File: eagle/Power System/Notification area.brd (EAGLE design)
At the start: 114 x 80 mm, 53 parts, among them IC3 LM358N, T7 2N2222

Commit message: PCB layout beta
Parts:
- removed D5, D6, D7, D8: 1N4004, diode:DO41-10
- removed S1, S2: RDT1034, switch:RDT1034
- removed S4: TL32PO, switch:TL3XPO
- added C8, C9: 2uF, capacitor-wima:C2.5-3
- added LED_A: BLUE, display-hp:HLMP6
- added LED_B, LED_D: GREEN, display-hp:HLMP6
- added LED_C: RED, display-hp:HLMP6
- added PAD3: Power +, wirepad:5-2,5
- added PAD4: Power -, wirepad:5-2,5
- added SV2: (no value), con-lstb:MA03-1
- added U$1, U$2, U$4: (no value), holes:3,0
- C4, C7: value 1uF -> 2uF
- D1, D2: value HLMP6 -> 1N4001; device display-hp:HLMP6 -> diode:DO41-10
- D3, D4: value HLMP6 -> 1N4004; device display-hp:HLMP6 -> diode:DO41-10
- PAD1: value WIREPADSMD5-2,5 -> Motor +
- PAD2: value WIREPADSMD5-2,5 -> Motor -
- moved D9 211.0 mm to (99.1, 38.1)
- moved R20 206.5 mm to (67.3, 62.2)
- moved R18 188.6 mm to (67.3, 57.1), turned to 180 degrees
- moved R16 183.4 mm to (57.1, 64.8), turned to 180 degrees
- moved R14 177.6 mm to (57.1, 59.7), turned to 180 degrees
- moved R19 176.5 mm to (54.6, 49.5), turned to 90 degrees
- moved T7 173.4 mm to (47.0, 48.3), turned to 180 degrees
- moved T6 171.6 mm to (61.0, 49.5)
- moved R12 164.8 mm to (90.2, 35.6), turned to 270 degrees
- moved T5 162.0 mm to (97.8, 31.8), turned to 180 degrees
- moved R9 146.4 mm to (77.5, 61.0), turned to 180 degrees
- moved SV1 146.2 mm to (54.6, 71.1)
- moved R8 144.2 mm to (78.7, 26.7), turned to 270 degrees
- moved IC3 144.0 mm to (47.0, 58.4), turned to 90 degrees
- moved R2 137.8 mm to (76.2, 26.7), turned to 90 degrees
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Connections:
- removed net N$15: S1.B, S2.B
- removed net V-: IC3.4
- new net N$29: R20.1, T7.2
- new net N$30: C8.2, C9.1
- new net N$31: R7.2, T4.C
- new net N$32: R1.1, T1.C
- new net N$33: R3.2, T2.C
- net +3V3: now also D2.C, LED_A.A, LED_B.A, LED_C.A, LED_D.A; no longer D2.A, D3.A, D4.A, D5.C, D6.A
- net +5V: now also C8.1, D3.A, D4.C; no longer C7.1, D7.C, D8.A
- net GND: now also C9.2, IC3.4, PAD4.1, SV2.3; no longer C4.2
- net N$1: now also LED_C.K; no longer D1.K
- net N$13: now also SV2.1; no longer S1.A, S2.A
- net N$14: now also R5.1, T3.C; no longer C2.1, C5.1, D6.C, D8.C, IC1.3, IC2.3, PAD1.1, S4.2
- net N$17: now also C4.2, C7.1; no longer S1.A1, S2.A1
- net N$19: now also D2.A; no longer D5.A
- net N$20: now also D4.A; no longer D7.A
- net N$28: now also R20.2; no longer R20.1, T7.2
- net N$3: now also LED_D.K; no longer D2.K
- net N$5: now also LED_A.K; no longer D3.K
- net N$7: now also LED_B.K; no longer D4.K
- net V+: now also C2.1, C5.1, D1.C, D3.C, IC1.3, IC2.3, PAD1.1, PAD3.1; no longer S4.3
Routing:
- net +5V: track 0.00 -> 215.5 mm
- net V+: track 0.00 -> 159.3 mm
- net +3V3: track 0.00 -> 123.6 mm
- net N$9: track 0.00 -> 102.4 mm
- net N$11: track 0.00 -> 97.3 mm
- net N$18: track 0.00 -> 91.5 mm
- net N$12: track 0.00 -> 85.7 mm
- net N$24: track 0.00 -> 79.7 mm
- net N$29: track 0.00 -> 47.4 mm
- net N$6: track 0.00 -> 45.0 mm
- net N$21: track 0.00 -> 44.2 mm
- net N$8: track 0.00 -> 34.3 mm
- net N$26: track 0.00 -> 33.9 mm
- net N$19: track 0.00 -> 28.9 mm
- net N$20: track 0.00 -> 27.3 mm
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- added copper zone on layer 1, net GND
- added copper zone on layer 16, net GND
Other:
- board size 114 x 80 mm -> 112.7 x 80 mm

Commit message: updated pcb
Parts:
- SG1: value F/BC35 -> F/DB18; device buzzer:F/BC35 -> buzzer:F/DB18
- moved SG1 16.9 mm to (84.7, 50.8)
- moved U$4 11.4 mm to (105.7, 11.0)
- moved U$1 7.79 mm to (10.8, 10.7)
- moved R12 5.21 mm to (90.0, 30.4)
- moved T5 3.59 mm to (98.3, 28.2)
- moved U$2 2.42 mm to (106.6, 73.5)
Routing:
- net N$21: track 44.2 -> 0.00 mm
- net +5V: track 215.5 -> 189.8 mm
- net N$16: track 11.0 -> 0.00 mm
- net N$24: track 79.7 -> 72.0 mm
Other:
- board size 112.7 x 80 mm -> 110.7 x 80.3 mm
- board text added: "Jose A. Montes Perez Enrique J. Torres Rivera Leroy Y. Gonzalez Torres ICOM 4217"

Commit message: final pcb versions
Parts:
- moved U$2 98.5 mm to (9.83, 92.0)
- moved PAD3 87.5 mm to (70.4, 8.89), turned to 0 degrees
- moved C2 76.6 mm to (64.5, 8.57), turned to 180 degrees
- moved R6 71.6 mm to (24.1, 69.8), turned to 270 degrees
- moved PAD4 70.1 mm to (58.4, 8.89), turned to 0 degrees
- moved PAD1 61.2 mm to (52.1, 8.89), turned to 0 degrees
- moved R8 61.1 mm to (35.6, 69.8), turned to 90 degrees
- moved T3 55.7 mm to (19.1, 76.2)
- moved C5 54.0 mm to (47.0, 8.89), turned to 180 degrees
- moved T4 53.8 mm to (30.5, 76.2)
- moved T1 51.8 mm to (44.5, 76.2)
- moved LED_A 51.4 mm to (19.1, 87.6)
- moved R5 51.4 mm to (16.5, 82.5)
- moved T2 51.4 mm to (53.3, 76.2)
- moved R2 50.8 mm to (49.5, 69.8), turned to 270 degrees
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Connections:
- new net N$34: R10.1, SV2.2
- net N$12: now also SV1.6; no longer SV1.7
- net N$13: no longer R10.1
- net N$18: now also SV1.7; no longer SV1.6
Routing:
- net V+: track 159.3 -> 266.8 mm
- net +3V3: track 123.6 -> 216.0 mm
- net N$28: track 14.3 -> 76.3 mm
- net N$12: track 85.7 -> 31.1 mm
- net N$18: track 91.5 -> 44.6 mm
- net N$11: track 97.3 -> 51.4 mm
- net N$9: track 102.4 -> 60.3 mm
- net N$6: track 45.0 -> 4.58 mm
- net +5V: track 189.8 -> 150.1 mm
- net N$20: track 27.3 -> 62.3 mm
- net N$8: track 34.3 -> 4.58 mm
- net N$10: track 25.5 -> 49.4 mm
- net N$16: track 0.00 -> 21.0 mm
- net N$29: track 47.4 -> 28.6 mm
- net N$2: track 23.2 -> 4.58 mm
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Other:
- board size 110.7 x 80.3 mm -> 100.2 x 97.8 mm

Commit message: final final final eagle files
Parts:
- moved U$2 1.71 mm to (9.19, 90.4)
- moved U$1 0.90 mm to (9.50, 6.43)
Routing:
- net +5V: track 150.1 -> 147.1 mm
- net V+: track 266.8 -> 268.8 mm
- net N$34: track 6.66 -> 7.77 mm
- net N$6: track 4.58 -> 5.61 mm
- net N$8: track 4.58 -> 5.61 mm
- net N$4: track 4.58 -> 5.61 mm
- net N$2: track 4.58 -> 5.61 mm
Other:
- board size 100.2 x 97.8 mm -> 99.1 x 96.5 mm
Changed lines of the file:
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@@
 <?xml version="1.0" encoding="utf-8"?>
 <!DOCTYPE eagle SYSTEM "eagle.dtd">
-<eagle version="7.5.0">
+<eagle version="7.3.0">
 <drawing>
 <settings>
@@
 <layer number="155" name="FabDoc3" color="7" fill="1" visible="yes" active="yes"/>
 <layer number="199" name="Contour" color="7" fill="1" visible="yes" active="yes"/>
-<layer number="200" name="200bmp" color="1" fill="10" visible="no" active="yes"/>
+<layer number="200" name="200bmp" color="1" fill="10" visible="yes" active="yes"/>
 <layer number="201" name="201bmp" color="2" fill="10" visible="yes" active="yes"/>
 <layer number="202" name="202bmp" color="3" fill="10" visible="yes" active="yes"/>
@@
 <board>
 <plain>
-<wire x1="1.27" y1="0" x2="101.4605" y2="0.0635" width="0" layer="20"/>
-<wire x1="101.4605" y1="0.0635" x2="101.4605" y2="97.8435" width="0" layer="20"/>
-<wire x1="101.4605" y1="97.8435" x2="1.27" y2="97.78" width="0" layer="20"/>
-<wire x1="1.27" y1="97.78" x2="1.27" y2="0" width="0" layer="20"/>
 <rectangle x1="30.3149" y1="45.4787" x2="32.0929" y2="45.6057" layer="200" rot="R180"/>
 <rectangle x1="27.6479" y1="45.4787" x2="28.9179" y2="45.6057" layer="200" rot="R180"/>
@@
 <rectangle x1="79.7306" y1="80.5942" x2="82.3722" y2="80.645" layer="200" rot="R180"/>
 <rectangle x1="80.2894" y1="80.645" x2="81.8134" y2="80.6958" layer="200" rot="R180"/>
+<wire x1="2.54" y1="0" x2="2.54" y2="96.52" width="0" layer="20"/>
+<wire x1="2.54" y1="96.52" x2="101.6" y2="96.52" width="0" layer="20"/>
+<wire x1="101.6" y1="96.52" x2="101.6" y2="0" width="0" layer="20"/>
+<wire x1="101.6" y1="0" x2="2.54" y2="0" width="0" layer="20"/>
 </plain>
 <attributes>
@@
 <attribute name="VALUE" x="31.6865" y="26.797" size="1.27" layer="27" ratio="10"/>
 </element>
-<element name="U$1" library="holes" package="3,0" value="" x="10.1346" y="7.0612"/>
-<element name="U$2" library="holes" package="3,0" value="" x="9.8298" y="91.9734"/>
+<element name="U$1" library="holes" package="3,0" value="" x="9.4996" y="6.4262"/>
+<element name="U$2" library="holes" package="3,0" value="" x="9.1948" y="90.3859"/>
 <element name="U$4" library="holes" package="3,0" value="" x="94.996" y="6.8834"/>
 <element name="SG1" library="buzzer" package="F/DB18" value="F/DB18" x="83.693" y="26.67" rot="R270">
@@
 <contactref element="PAD4" pad="1"/>
 <contactref element="SV2" pad="3"/>
-<polygon width="0.4064" layer="16" spacing="1.778" pour="hatch" isolate="0.00030625">
-<vertex x="0" y="99.06"/>
-<vertex x="101.6" y="99.06"/>
-<vertex x="101.6" y="0"/>
-<vertex x="0" y="0"/>
-</polygon>
 <wire x1="57.15" y1="55.88" x2="62.23" y2="55.88" width="0.4064" layer="1"/>
 <wire x1="62.23" y1="55.88" x2="63.5" y2="54.61" width="0.4064" layer="1"/>
-<polygon width="0.4064" layer="1" spacing="1.778" pour="hatch" isolate="0.00030625">
-<vertex x="0" y="99.06"/>
-<vertex x="101.6" y="99.06"/>
+<polygon width="0.4064" layer="16">
+<vertex x="2.54" y="96.52"/>
+<vertex x="101.6" y="96.52"/>
+<vertex x="101.6" y="0"/>
+<vertex x="2.54" y="0"/>
+</polygon>
+<polygon width="0.4064" layer="1">
+<vertex x="2.54" y="96.52"/>
+<vertex x="101.6" y="96.52"/>
 <vertex x="101.6" y="0"/>
-<vertex x="0" y="0"/>
+<vertex x="2.54" y="0"/>
 </polygon>
 </signal>
@@
 <contactref element="T1" pad="B"/>
 <contactref element="R2" pad="1"/>
-<wire x1="49.53" y1="73.66" x2="45.72" y2="76.2" width="0.4064" layer="1"/>
+<wire x1="49.53" y1="73.66" x2="49.53" y2="74.93" width="0.4064" layer="1"/>
+<wire x1="49.53" y1="74.93" x2="48.26" y2="76.2" width="0.4064" layer="1"/>
+<wire x1="48.26" y1="76.2" x2="45.72" y2="76.2" width="0.4064" layer="1"/>
 </signal>
 <signal name="N$3">
@@
 <contactref element="T2" pad="B"/>
 <contactref element="R4" pad="2"/>
-<wire x1="58.42" y1="73.66" x2="54.61" y2="76.2" width="0.4064" layer="1"/>
+<wire x1="58.42" y1="73.66" x2="58.42" y2="74.93" width="0.4064" layer="1"/>
+<wire x1="58.42" y1="74.93" x2="57.15" y2="76.2" width="0.4064" layer="1"/>
+<wire x1="57.15" y1="76.2" x2="54.61" y2="76.2" width="0.4064" layer="1"/>
 </signal>
 <signal name="N$5">
@@
 <contactref element="T3" pad="B"/>
 <contactref element="R6" pad="1"/>
-<wire x1="20.32" y1="76.2" x2="24.13" y2="73.66" width="0.4064" layer="1"/>
+<wire x1="20.32" y1="76.2" x2="22.86" y2="76.2" width="0.4064" layer="1"/>
+<wire x1="22.86" y1="76.2" x2="24.13" y2="74.93" width="0.4064" layer="1"/>
+<wire x1="24.13" y1="74.93" x2="24.13" y2="73.66" width="0.4064" layer="1"/>
 </signal>
 <signal name="N$7">
@@
 <contactref element="T4" pad="B"/>
 <contactref element="R8" pad="2"/>
-<wire x1="31.75" y1="76.2" x2="35.56" y2="73.66" width="0.4064" layer="1"/>
+<wire x1="31.75" y1="76.2" x2="34.29" y2="76.2" width="0.4064" layer="1"/>
+<wire x1="34.29" y1="76.2" x2="35.56" y2="74.93" width="0.4064" layer="1"/>
+<wire x1="35.56" y1="74.93" x2="35.56" y2="73.66" width="0.4064" layer="1"/>
 </signal>
 <signal name="N$12">
@@
 <wire x1="35.56" y1="35.56" x2="34.29" y2="35.56" width="0.4064" layer="16"/>
 <wire x1="34.29" y1="35.56" x2="31.75" y2="33.02" width="0.4064" layer="16"/>
-<wire x1="75.819" y1="22.479" x2="71.12" y2="17.78" width="0.4064" layer="1"/>
+<wire x1="72.3265" y1="19.6215" x2="71.12" y2="17.78" width="0.4064" layer="1"/>
 <wire x1="71.12" y1="17.78" x2="60.96" y2="17.78" width="0.4064" layer="1"/>
 <wire x1="60.96" y1="17.78" x2="58.42" y2="20.32" width="0.4064" layer="1"/>
@@
 <wire x1="72.7456" y1="37.4904" x2="76.2" y2="40.9448" width="0.4064" layer="16"/>
 <wire x1="76.2" y1="40.9448" x2="76.2" y2="58.42" width="0.4064" layer="16"/>
-<wire x1="75.819" y1="22.479" x2="75.819" y2="33.9344" width="0.4064" layer="1"/>
-<wire x1="75.819" y1="33.9344" x2="72.263" y2="37.4904" width="0.4064" layer="1"/>
+<wire x1="72.3265" y1="19.6215" x2="72.3265" y2="27.2669" width="0.4064" layer="1"/>
+<wire x1="72.3265" y1="27.2669" x2="72.263" y2="37.4904" width="0.4064" layer="1"/>
 <wire x1="71.12" y1="63.5" x2="71.12" y2="68.58" width="0.4064" layer="16"/>
 <wire x1="71.12" y1="68.58" x2="68.58" y2="71.12" width="0.4064" layer="16"/>
@@
 <wire x1="15.24" y1="15.24" x2="20.32" y2="10.16" width="0.4064" layer="1"/>
 <wire x1="20.32" y1="10.16" x2="27.94" y2="10.16" width="0.4064" layer="1"/>
-<wire x1="27.94" y1="10.16" x2="35.56" y2="2.54" width="0.4064" layer="1"/>
-<wire x1="35.56" y1="2.54" x2="46.99" y2="2.54" width="0.4064" layer="1"/>
-<wire x1="46.99" y1="2.54" x2="52.07" y2="7.62" width="0.4064" layer="1"/>
+<wire x1="27.94" y1="10.16" x2="35.56" y2="5.08" width="0.4064" layer="1"/>
+<wire x1="35.56" y1="5.08" x2="49.2125" y2="5.08" width="0.4064" layer="1"/>
+<wire x1="49.2125" y1="5.08" x2="52.07" y2="7.62" width="0.4064" layer="1"/>
 <wire x1="26.67" y1="57.15" x2="30.48" y2="53.34" width="0.4064" layer="1"/>
 <wire x1="30.48" y1="53.34" x2="30.48" y2="43.18" width="0.4064" layer="1"/>
@@
 <wire x1="63.5" y1="33.02" x2="66.04" y2="33.02" width="0.4064" layer="16"/>
 <wire x1="66.04" y1="33.02" x2="68.58" y2="30.48" width="0.4064" layer="16"/>
-<wire x1="68.58" y1="30.48" x2="68.58" y2="25.4" width="0.4064" layer="16"/>
-<wire x1="68.58" y1="25.4" x2="71.12" y2="22.86" width="0.4064" layer="16"/>
-<wire x1="71.12" y1="22.86" x2="71.12" y2="9.652" width="0.4064" layer="16"/>
-<wire x1="71.12" y1="9.652" x2="70.358" y2="8.89" width="0.4064" layer="16"/>
+<wire x1="68.58" y1="30.48" x2="68.58" y2="26.67" width="0.4064" layer="16"/>
+<wire x1="68.58" y1="26.67" x2="71.12" y2="24.13" width="0.4064" layer="16"/>
+<wire x1="71.12" y1="24.13" x2="71.12" y2="9.652" width="0.4064" layer="16"/>
 <wire x1="66.04" y1="35.56" x2="66.04" y2="35.6108" width="0.4064" layer="16"/>
 <wire x1="66.04" y1="35.6108" x2="69.9516" y2="39.5224" width="0.4064" layer="16"/>
 <wire x1="69.9516" y1="39.5224" x2="69.9516" y2="45.9232" width="0.4064" layer="16"/>
 <wire x1="69.9516" y1="45.9232" x2="72.7964" y2="48.768" width="0.4064" layer="16"/>
-<wire x1="70.358" y1="8.89" x2="70.358" y2="8.89" width="0" layer="19" extent="1-16"/>
+<wire x1="71.12" y1="9.652" x2="70.358" y2="8.89" width="0.4064" layer="16"/>
+<wire x1="70.358" y1="8.89" x2="66.04" y2="8.89" width="0.4064" layer="16"/>
+<wire x1="66.04" y1="8.89" x2="65.7225" y2="8.5725" width="0.4064" layer="16"/>
 </signal>
 <signal name="N$18">
@@
 <contactref element="R10" pad="1"/>
 <contactref element="SV2" pad="2"/>
-<wire x1="92.71" y1="58.42" x2="93.98" y2="58.42" width="0.4064" layer="1"/>
-<wire x1="93.98" y1="58.42" x2="97.79" y2="54.61" width="0.4064" layer="1"/>
+<wire x1="92.71" y1="58.42" x2="92.71" y2="56.515" width="0.4064" layer="1"/>
+<wire x1="92.71" y1="56.515" x2="94.615" y2="54.61" width="0.4064" layer="1"/>
+<wire x1="94.615" y1="54.61" x2="97.79" y2="54.61" width="0.4064" layer="1"/>
 </signal>
 </signals>

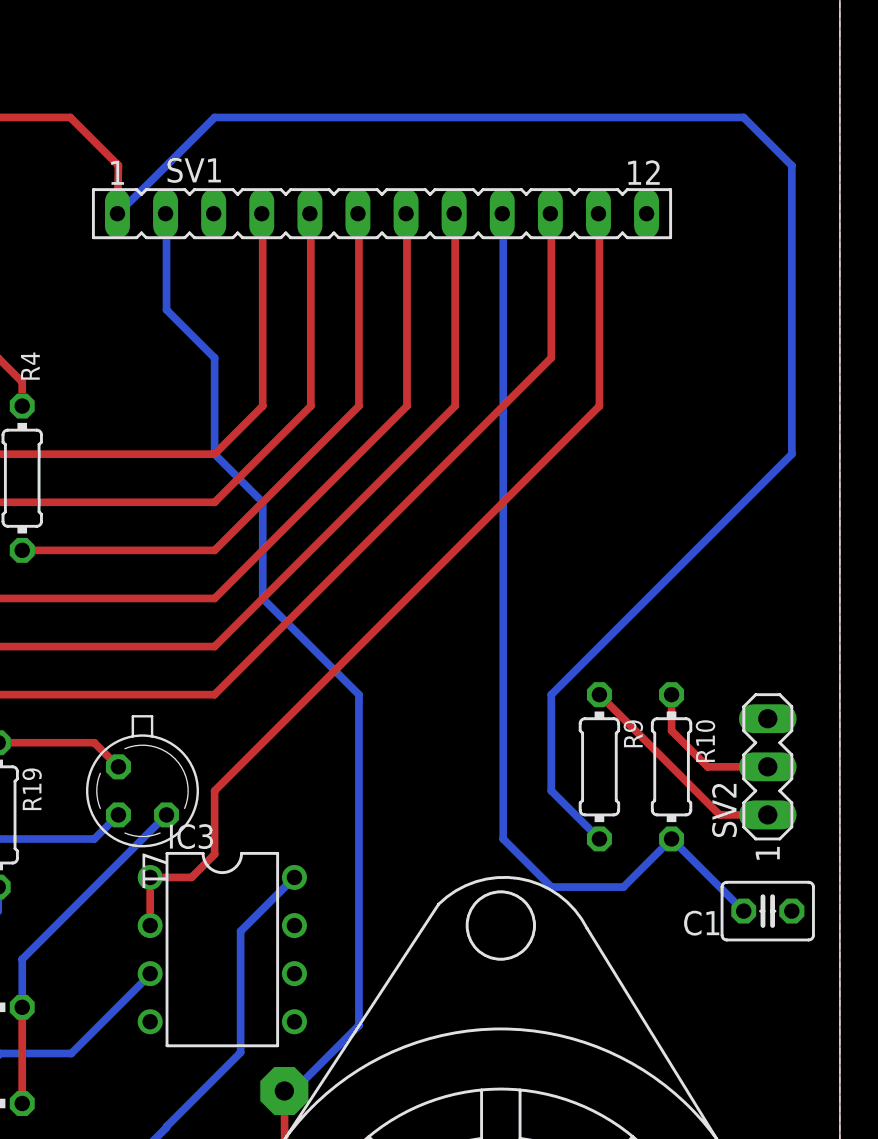
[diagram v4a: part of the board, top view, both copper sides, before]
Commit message: added multimeter
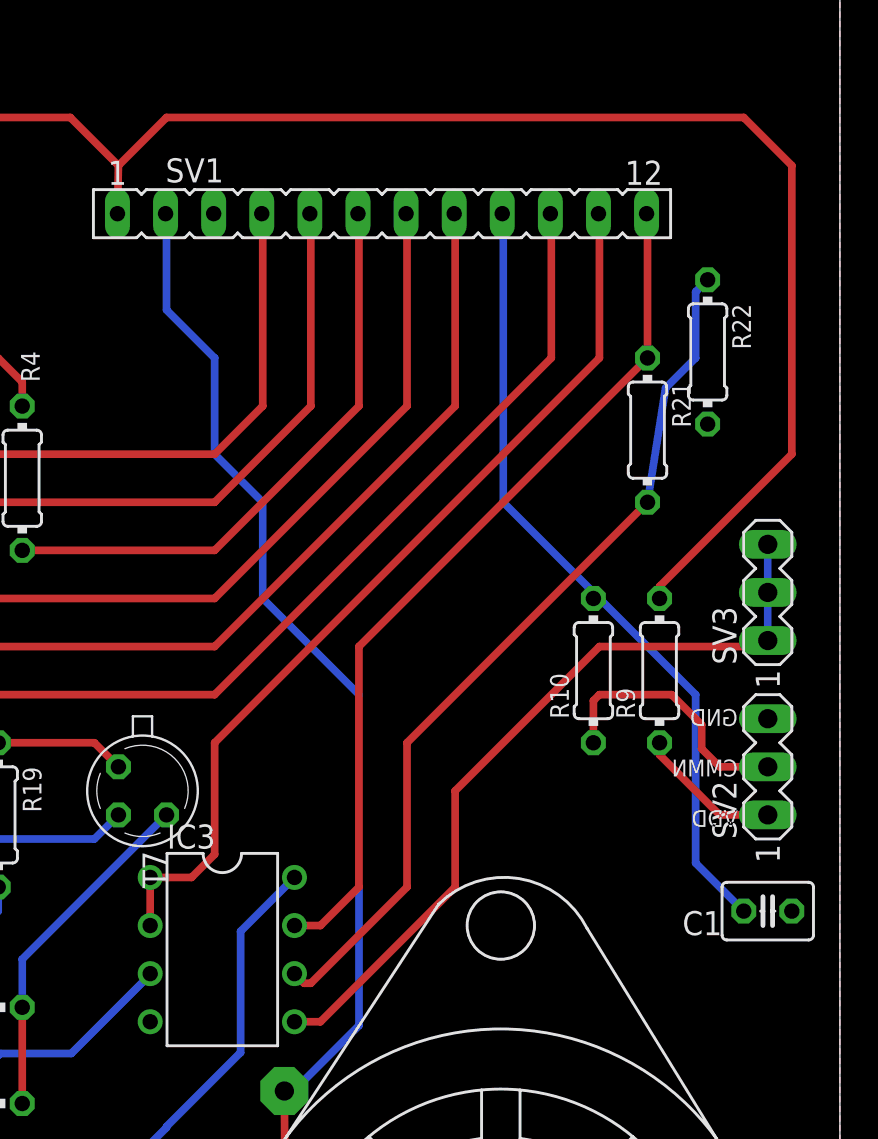
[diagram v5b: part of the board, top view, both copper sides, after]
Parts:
- added R21: 13K, rcl:0204/7
- added R22: 1K, rcl:0204/7
- added SV3: (no value), con-lstb:MA03-1
- moved R10 6.55 mm to (88.6, 59.7), turned to 90 degrees
- moved R9 5.99 mm to (92.1, 59.7), turned to 90 degrees
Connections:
- new net N$35: IC3.6, R21.2, R22.1
- new net N$36: IC3.7, R21.1, SV1.12
- new net N$37: IC3.5, SV3.1, SV3.2, SV3.3
- net GND: now also R22.2
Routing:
- net N$35: track 0.00 -> 46.6 mm
- net N$36: track 0.00 -> 46.2 mm
- net N$37: track 0.00 -> 41.4 mm
- net +3V3: track 216.0 -> 198.8 mm
- net N$10: track 49.4 -> 42.3 mm
- net N$34: track 7.77 -> 13.9 mm
- net N$13: track 11.5 -> 7.67 mm
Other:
- board text added: "GND CMMN VDD"
